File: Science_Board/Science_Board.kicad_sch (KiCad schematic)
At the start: 55 parts, among them J1 Conn_01x02, J10 Conn_01x02, J11 Conn_01x03, J12 Conn_01x03, J13 Conn_01x03, J14 Conn_01x03, J15 Conn_01x03, J16 Conn_01x03, J17 Conn_01x03, J18 Conn_01x03, J19 Conn_01x02, J2 RJ45_LED_Shielded, J20 Molex_Megafit_02, J22 Molex_Megafit_02, J23 Conn_01x02, J5 Conn_01x05, J6 Conn_01x04, J7 Conn_01x03, J8 Conn_01x03, J9 Conn_01x02, Q5 NMOS, SW1 SW_Push, SW10 SW_Push, SW11 SW_Push, SW12 SW_SPDT, SW2 SW_Push, SW3 SW_Push, SW4 SW_Push, SW5 SW_Push, SW6 SW_Push, SW7 SW_Push, SW8 SW_Push, SW9 SW_Push, U5 PCA9685BS

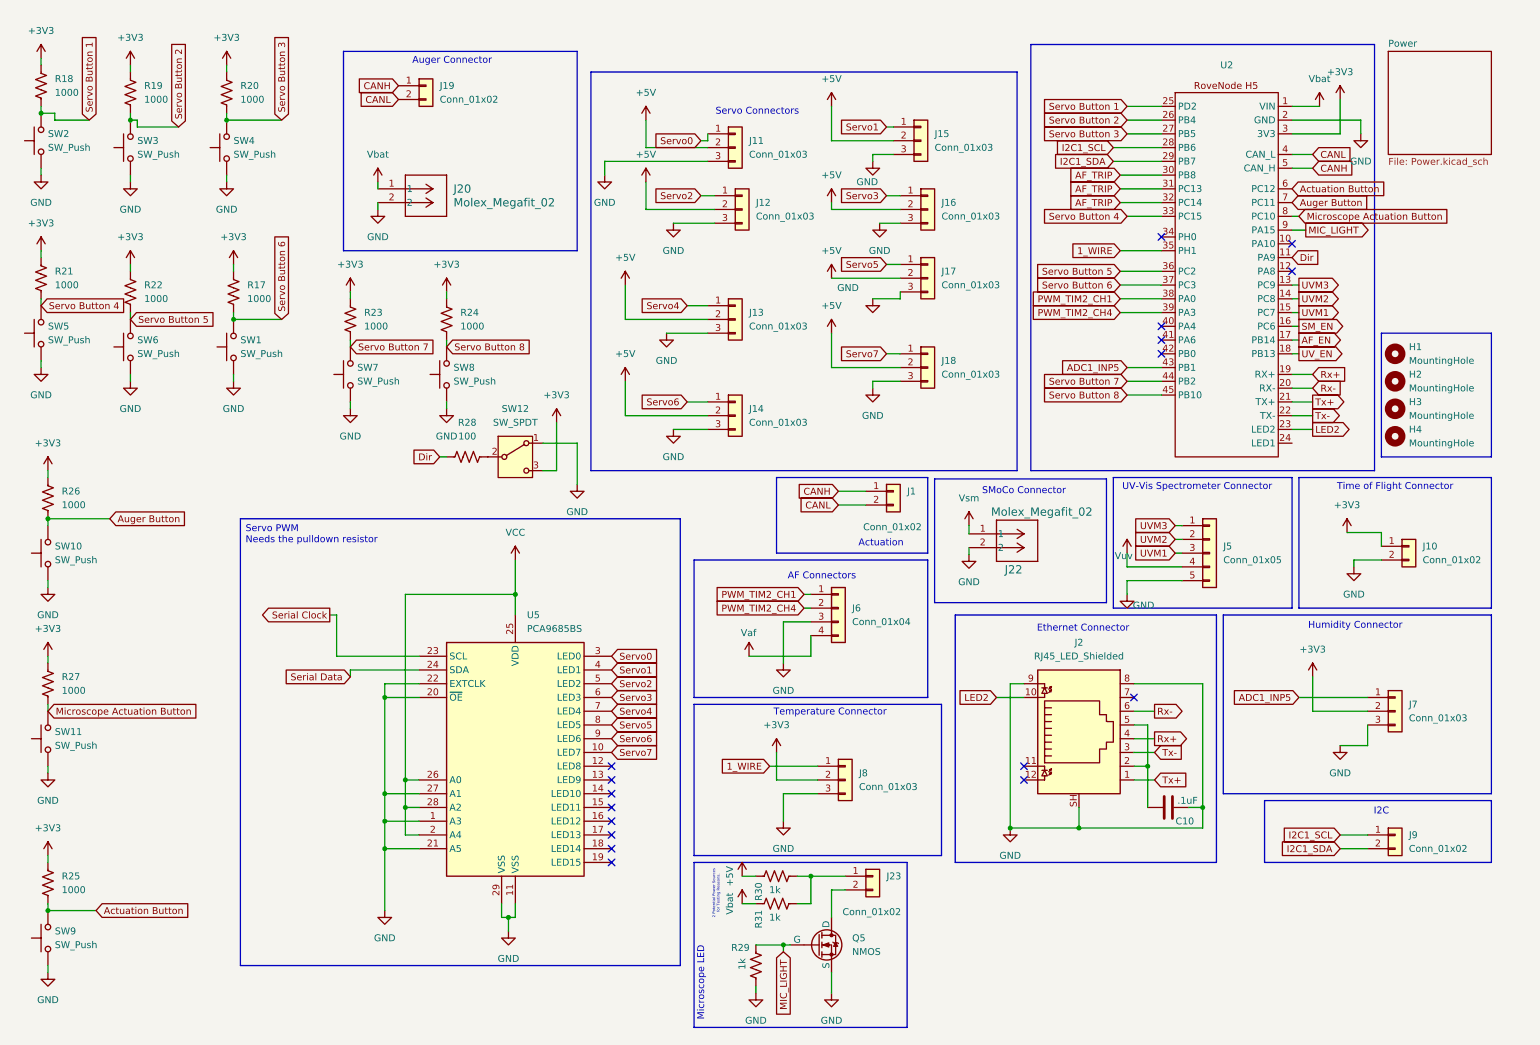
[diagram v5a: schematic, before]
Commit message: fixed some mistakes like making a box for buttons and the voltage flag being wrong for PWM driver
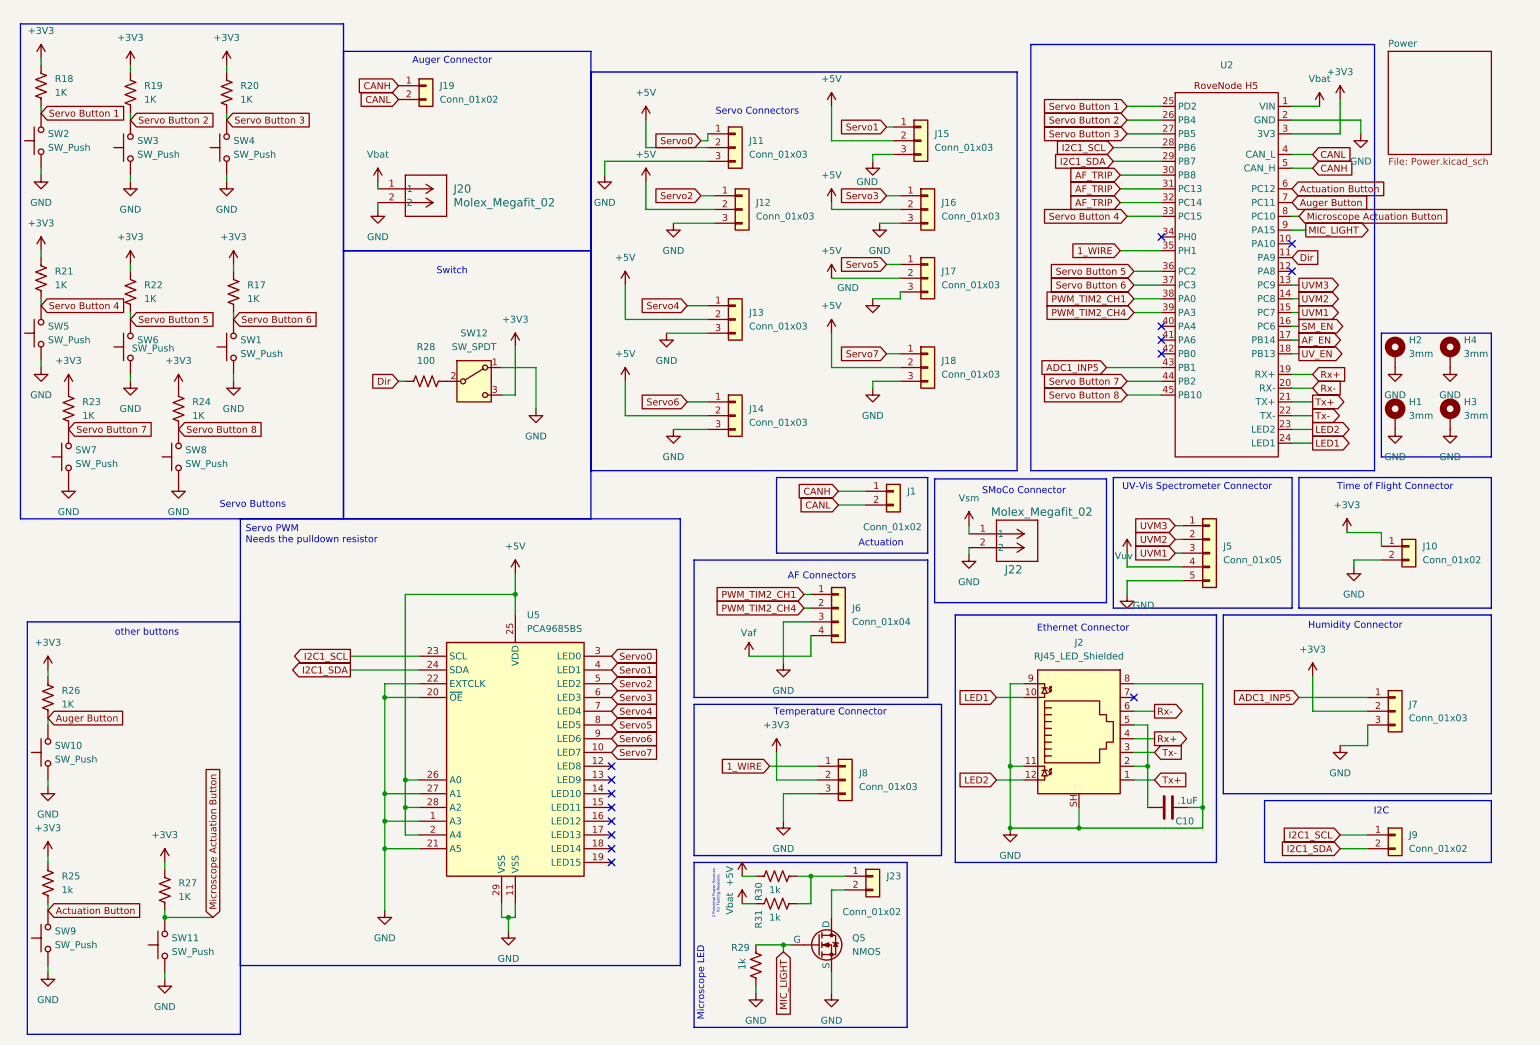
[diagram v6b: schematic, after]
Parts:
- removed H1, H2, H3, H4: MountingHole, symbol Mechanical:MountingHole
- added H1, H2, H3, H4: 3mm, MountingHole:MountingHole_3mm_Pad_Via, symbol Mechanical:MountingHole_Pad
- R17, R18, R19, R20, R21, R22, R23, R24, R26, R27: value 1000 -> 1K
- R25: value 1000 -> 1k
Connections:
- net Serial Clock is gone; now on net I2C1_SCL: U5.23 (SCL)
- net Serial Data is gone; now on net I2C1_SDA: U5.24 (SDA)
- net VCC is gone; now on net +5V: U5.2 (A4), U5.25 (VDD), U5.26 (A0), U5.28 (A2)
- net GND: now also J2.11, H1.1, H2.1, H3.1, H4.1
- net LED2: now also J2.12; no longer J2.10
- net LED1: now reaches U2.24 (LED1)
- net LED1: now also J2.10
- no-connect marks 17 -> 15
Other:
- note added: "Servo Buttons"
- note added: "Switch"
- note added: "other buttons"
- moved on the sheet: R23, R24, R26, R27, R28, SW10, SW11, SW12, SW7, SW8

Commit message: created decoupling capacitors
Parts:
- added C14, C16: 0.1uF, symbol Device:C
- added C15: 10uf, symbol Device:C
- added C17: 10uF, symbol Device:C
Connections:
- net +5V: now also C14.1, C15.2
- net GND: now also C14.2, C15.1, C16.2, C17.1
- net Vbat: now also C16.1, C17.2
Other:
- moved on the sheet: R18, SW2

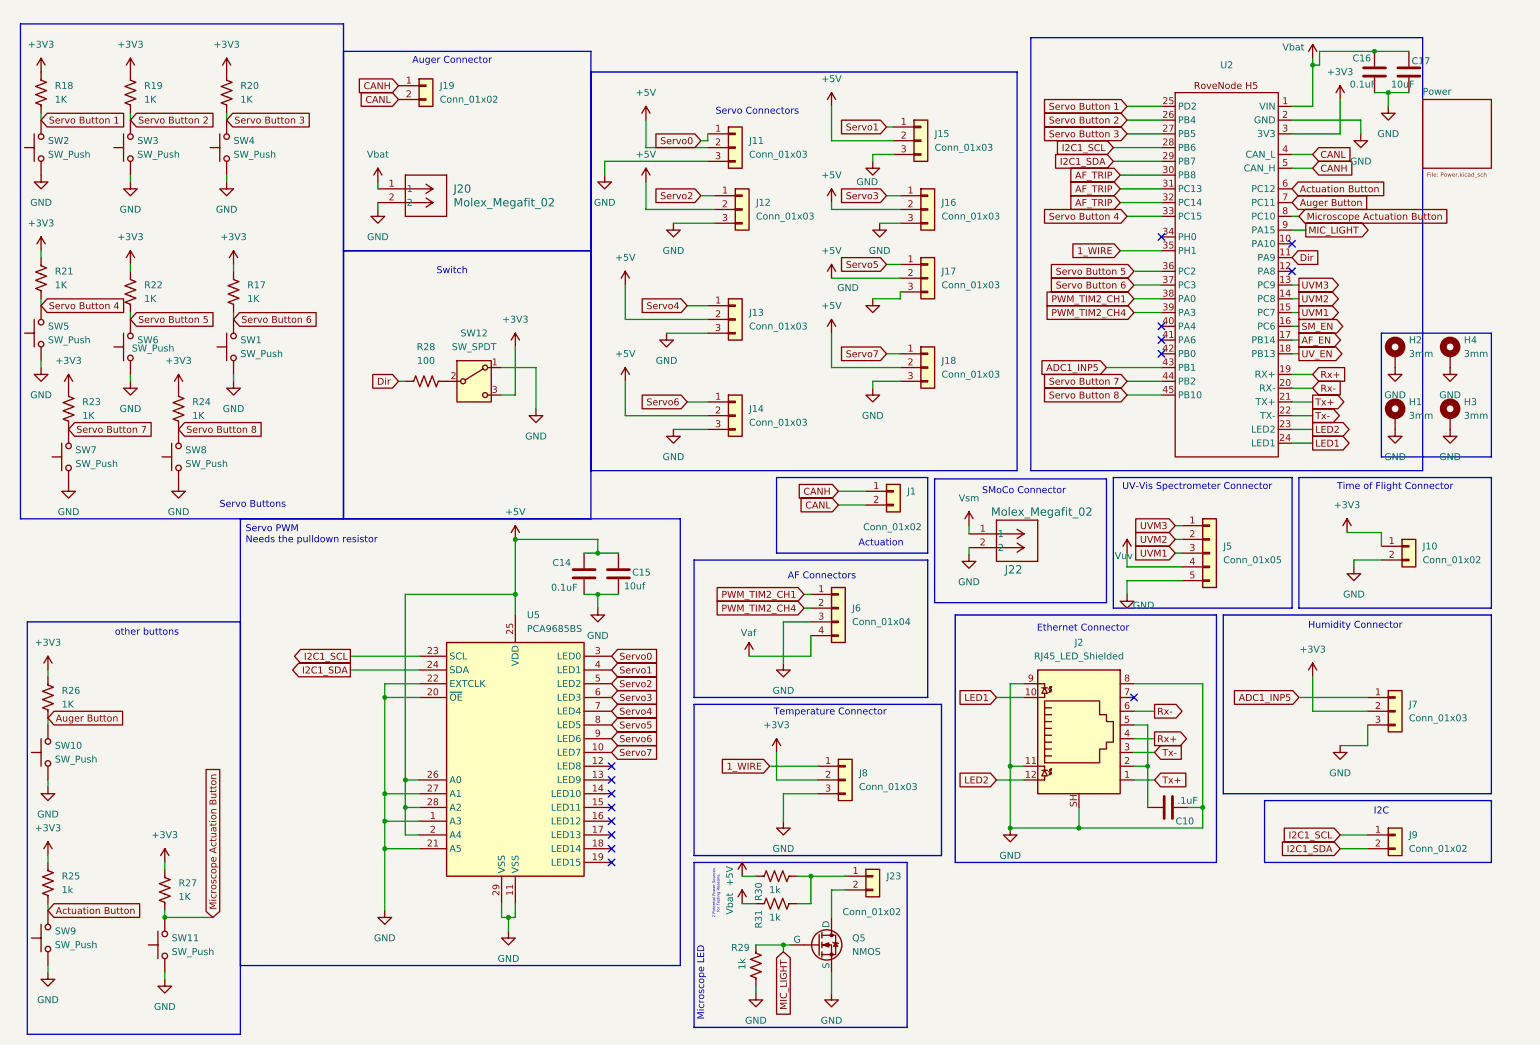
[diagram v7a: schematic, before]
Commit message: Fixed more like changing Vbat to +PV
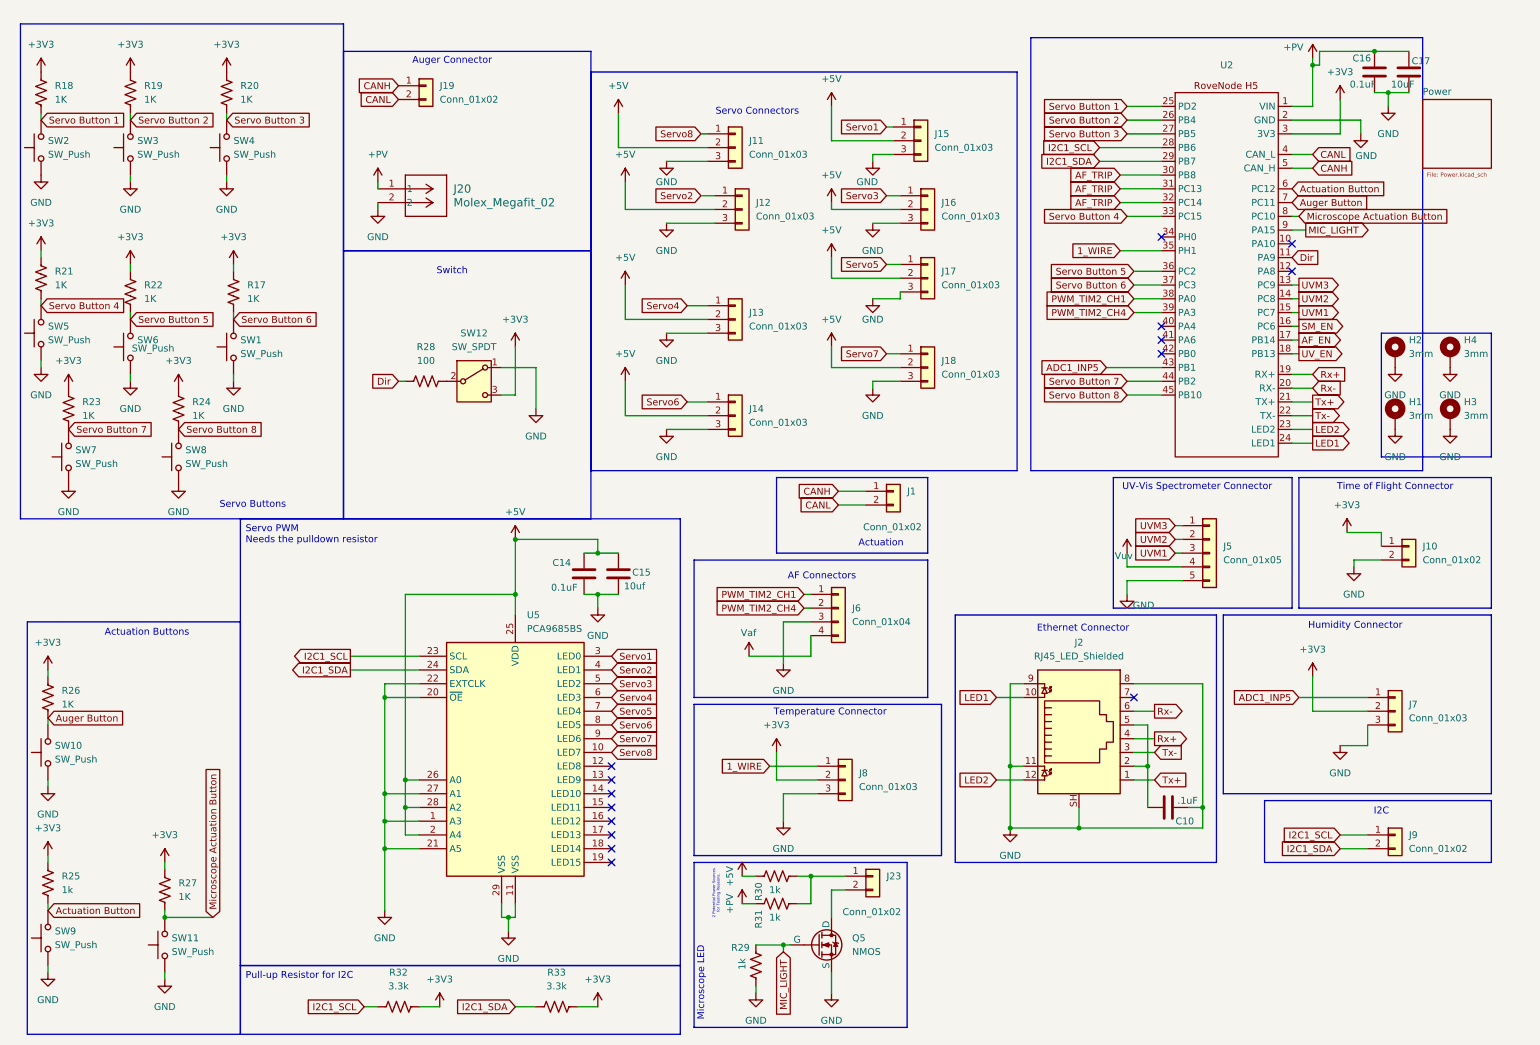
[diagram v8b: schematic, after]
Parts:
- removed J22: Molex_Megafit_02, MRDT_Connectors:MOLEX_MegaFit_02_Horizontal, symbol MRDT_Connectors:Molex_Megafit_02
- added R32, R33: 3.3k, Package_DIP:DIP-8_W7.62mm, symbol Device:R_US
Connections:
- net +3V3: now also R32.2, R33.2
- net I2C1_SCL: now also R32.1
- net I2C1_SDA: now also R33.1
- net Servo1: now also U5.3 (LED0); no longer U5.4 (LED1)
- net Servo2: now also U5.4 (LED1); no longer U5.5 (LED2)
- net Servo3: now also U5.5 (LED2); no longer U5.6 (LED3)
- net Servo4: now also U5.6 (LED3); no longer U5.7 (LED4)
- net Servo5: now also U5.7 (LED4); no longer U5.8 (LED5)
- net Servo6: now also U5.8 (LED5); no longer U5.9 (LED6)
- net Servo7: now also U5.9 (LED6); no longer U5.10 (LED7)
- net Servo0 renamed Servo8
- net Servo8: now also U5.10 (LED7); no longer U5.3 (LED0)
- net Vbat renamed +PV
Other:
- note added: "Actuation Buttons"
- note removed: "SMoCo Connector"
- note removed: "other buttons"
